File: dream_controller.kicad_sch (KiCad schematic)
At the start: 5 parts, among them J1 Conn_01x02_Male, J2 Conn_01x02_Male, U1 RP2040, U2 MCP2518FDT-H/SL, U3 MCP2561FD-E/SN

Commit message: added power
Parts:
- removed U2: MCP2518FDT-H/SL, SOIC14_150MIL_SL_MCH, symbol CAN IC:MCP2518FDT-H/SL
- removed U3: MCP2561FD-E/SN, SOIC8-N_MC_MCH, symbol TRANSCEIVER:MCP2561FD-E/SN
- added C1: 100u, symbol Device:C
- added C10, C?: 1u, symbol Device:C
- added C2, C3, C4, C5, C6, C7, C8, C9, C? (x2): 100n, symbol Device:C
- added R1: 1k, symbol Device:R_US
- added U2: W25Q32JVSS, Package_SO:SOIC-8_5.23x5.23mm_P1.27mm, symbol Memory_Flash:W25Q32JVSS
- added U3: MCP2518FDT-H/SL, SOIC14_150MIL_SL_MCH, symbol CAN IC:MCP2518FDT-H{brace}slash}SL
- added U4: MAX3051, symbol Interface_UART:MAX3051
- U1: footprint IC57_RP2040 -> RP2040_minimal:RP2040-QFN-56
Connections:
- net +3V3: now also U1.1 (IOVDD), U1.10 (IOVDD), U1.22 (IOVDD), U1.33 (IOVDD), U1.42 (IOVDD), U1.43 (ADC_AVDD), U1.44 (VREG_IN), U1.48 (USB_VDD), U1.49 (IOVDD), C1.1, C10.1, C2.1, C3.1, C4.1, C5.1, C6.1, C7.1, C8.1, C9.1, R1.1, U2.8 (VCC), U3.14 (VDD), U4.3 (VDD)
- net GND: now also U1.19 (TESTEN), U1.57 (GND), C1.2, C10.2, C2.2, C3.2, C4.2, C5.2, C6.2, C7.2, C8.2, C9.2, C?.2, C?.2, C?.2, U2.4 (GND), U3.7 (VSS), U4.2 (GND)
- net H_CAN: now also U4.7 (CANH)
- net L_CAN: now also U4.6 (CANL)
- net RX_CAN: now also U3.2 (RXCAN), U4.4 (RXD)
- net STBY: now also U3.9 (*INT0/GPIO0/XSTBY)
- net TX_CAN: now also U3.1 (TXCAN), U4.1 (TXD)
- net +1V1: now reaches U1.23 (DVDD)
- net +1V1: now also U1.45 (VREG_VOUT), U1.50 (DVDD), C?.1, C?.1, C?.1
- net F_D3: now reaches U1.51 (QSPI_SD3)
- net F_D3: now also U2.7 (IO3)
- net F_CLK: now reaches U1.52 (QSPI_SCLK)
- net F_CLK: now also U2.6 (CLK)
- net F_D0: now reaches U1.53 (QSPI_SD0)
- net F_D0: now also U2.5 (DI(IO0))
- net F_D2: now reaches U1.54 (QSPI_SD2)
- net F_D2: now also U2.3 (IO2)
- net F_D1: now reaches U1.55 (QSPI_SD1)
- net F_D1: now also U2.2 (DO(IO1))
- net SS: now reaches U1.56 (QSPI_SS)
- net SS: now also R1.2, U2.1 (~{CS})
- new net SHUTDOWN: U4.5 (SHDN)
- new net STANDBY: U4.8 (RS)

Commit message: update
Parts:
- added C14, C15: 14p, symbol Device:C
- added R1, R2: 27, symbol Device:R_US
- added Y1: Crystal, symbol Device:Crystal
- gave numbers to parts that had none: 3
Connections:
- net GND: now also C14.1, C15.1
- net at U1.20 (XIN): now also C14.2, Y1.1
- net at U1.21 (XOUT): now also C15.2, Y1.2
- net at U1.46 (USB_DM): now also R2.2
- net at U1.47 (USB_DP): now also R1.1
- new net D_N: R2.1
- new net D_P: R1.2

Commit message: added power for RP2040
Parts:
- added C? (x3): 10u, symbol Device:C
- added J1: USB_B_Micro, symbol Connector:USB_B_Micro
- added U5: LM1117-3.3, symbol Regulator_Linear:LM1117-3.3
- added U6: MAX40200AUK, Package_TO_SOT_SMD:SOT-23-5, symbol Analog_Switch:MAX40200AUK
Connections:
- net +3V3: now also C?.1, U5.2 (VO)
- net GND: now also C?.2, C?.2, C?.2, J1.5 (GND), J1.6 (Shield), U5.1 (GND), U6.2 (GND)
- net INHA: now reaches U1.2 (GPIO0)
- net INHB: now reaches U1.3 (GPIO1)
- net INLA: now reaches U1.4 (GPIO2)
- net INLB: now reaches U1.5 (GPIO3)
- net D_N renamed USB_D-
- net USB_D-: now also J1.2 (D-)
- net D_P renamed USB_D+
- net USB_D+: now also J1.3 (D+)
- new net: C?.1, J1.1 (VBUS), U6.1 (VDD), U6.3 (EN)
- new net VCC: C?.1, U5.3 (VI), U6.5 (OUT)
- no-connect marks 0 -> 1
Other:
- added sheet Driver (driver.kicad_sch)
- moved on the sheet: C1, R1, U2

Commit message: finished schematic design
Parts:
- removed C2, C3: 100n, symbol Device:C
- removed J1, J2: Conn_01x02_Male, symbol Connector:Conn_01x02_Male
- removed U3: MCP2518FDT-H/SL, SOIC14_150MIL_SL_MCH, symbol CAN IC:MCP2518FDT-H{brace}slash}SL
- removed U4: MAX3051, symbol Interface_UART:MAX3051
- added J2: Conn_01x04_Male, symbol Connector:Conn_01x04_Male
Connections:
- net INHA: now also U1.34 (GPIO22); no longer U1.2 (GPIO0)
- net INHB: now also U1.35 (GPIO23); no longer U1.3 (GPIO1)
- net INLA: now also U1.36 (GPIO24); no longer U1.4 (GPIO2)
- net INLB: now also U1.37 (GPIO25); no longer U1.5 (GPIO3)
- net CURRENT: now reaches U1.38 (GPIO26_ADC0)
- new net SPI_CLK: J2.2 (Pin_2), U1.4 (GPIO2)
- new net SPI_CS: J2.1 (Pin_1), U1.3 (GPIO1)
- new net SPI_MISO: J2.4 (Pin_4), U1.5 (GPIO3)
- new net SPI_MOSI: J2.3 (Pin_3), U1.2 (GPIO0)

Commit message: assigned footprints and started PCB
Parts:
- C1, C10, C11, C12, C13, C14, C15, C4, C5, C6, C7, C8, C9, R1, R2: footprint (none) -> Capacitor_SMD:C_0603_1608Metric
- C17, C2, C3: renamed from C?; footprint (none) -> Capacitor_SMD:C_0603_1608Metric
- J1: footprint (none) -> Connector_USB:USB_Micro-B_Amphenol_10118194_Horizontal
- J2: footprint (none) -> Connector_JST:JST_XH_B4B-XH-A_1x04_P2.50mm_Vertical
- R3: renamed from R1; footprint (none) -> Capacitor_SMD:C_0603_1608Metric
- U1: footprint RP2040_minimal:RP2040-QFN-56 -> RP2040:RP2040-QFN-56
- U5: footprint (none) -> Package_TO_SOT_SMD:SOT-223
- Y1: footprint (none) -> Crystal:Crystal_SMD_3225-4Pin_3.2x2.5mm
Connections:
- net XIN: now reaches C14.2, U1.20 (XIN), Y1.1
- net XOUT: now reaches C15.2, U1.21 (XOUT), Y1.2
- net VBUS: now reaches C2.1, J1.1 (VBUS), U6.1 (VDD), U6.3 (EN)
- net VCC renamed +15V

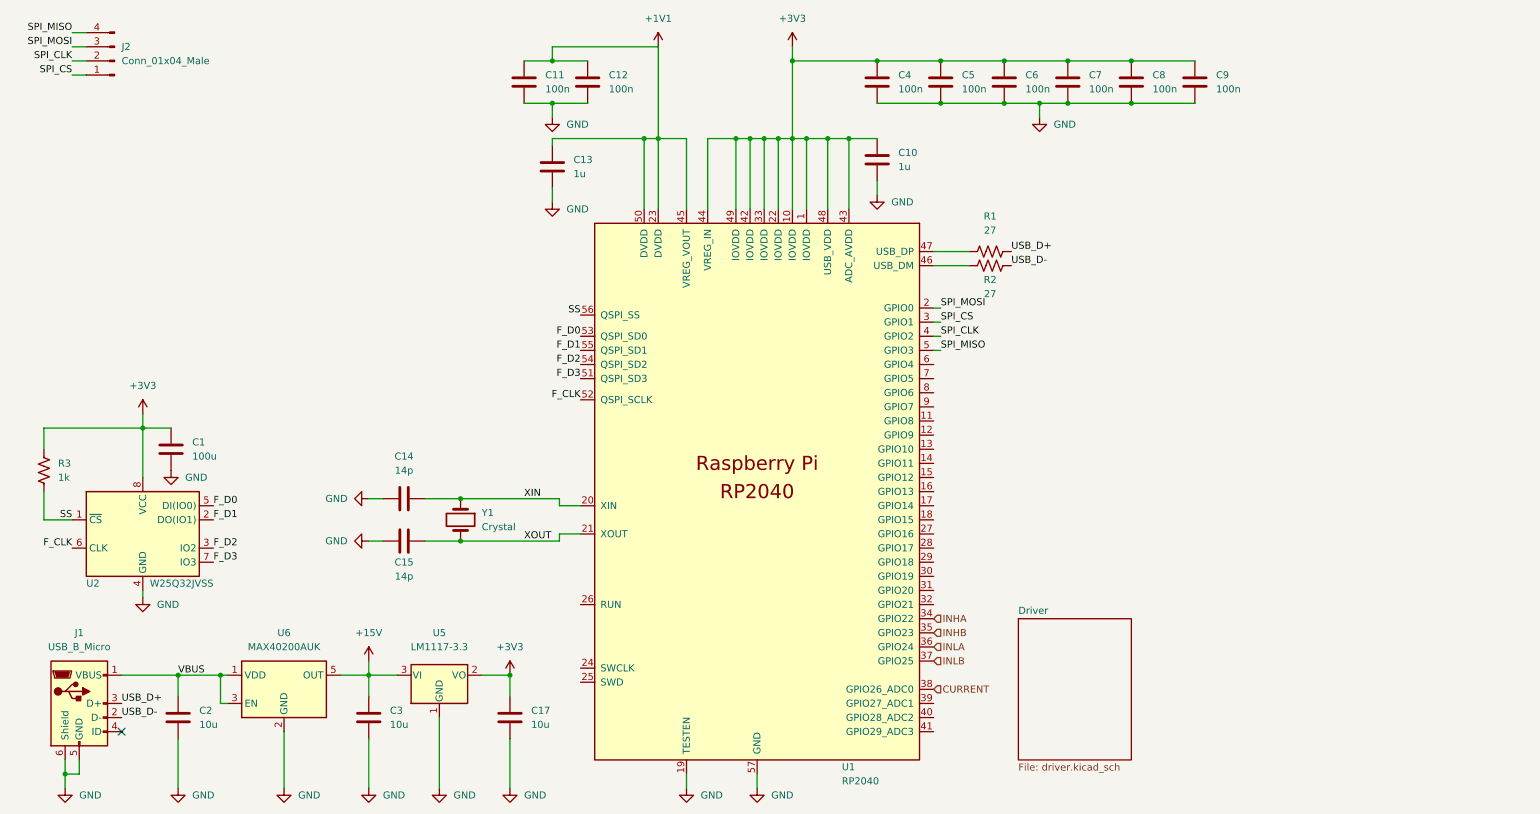
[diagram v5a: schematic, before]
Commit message: updating to CAN
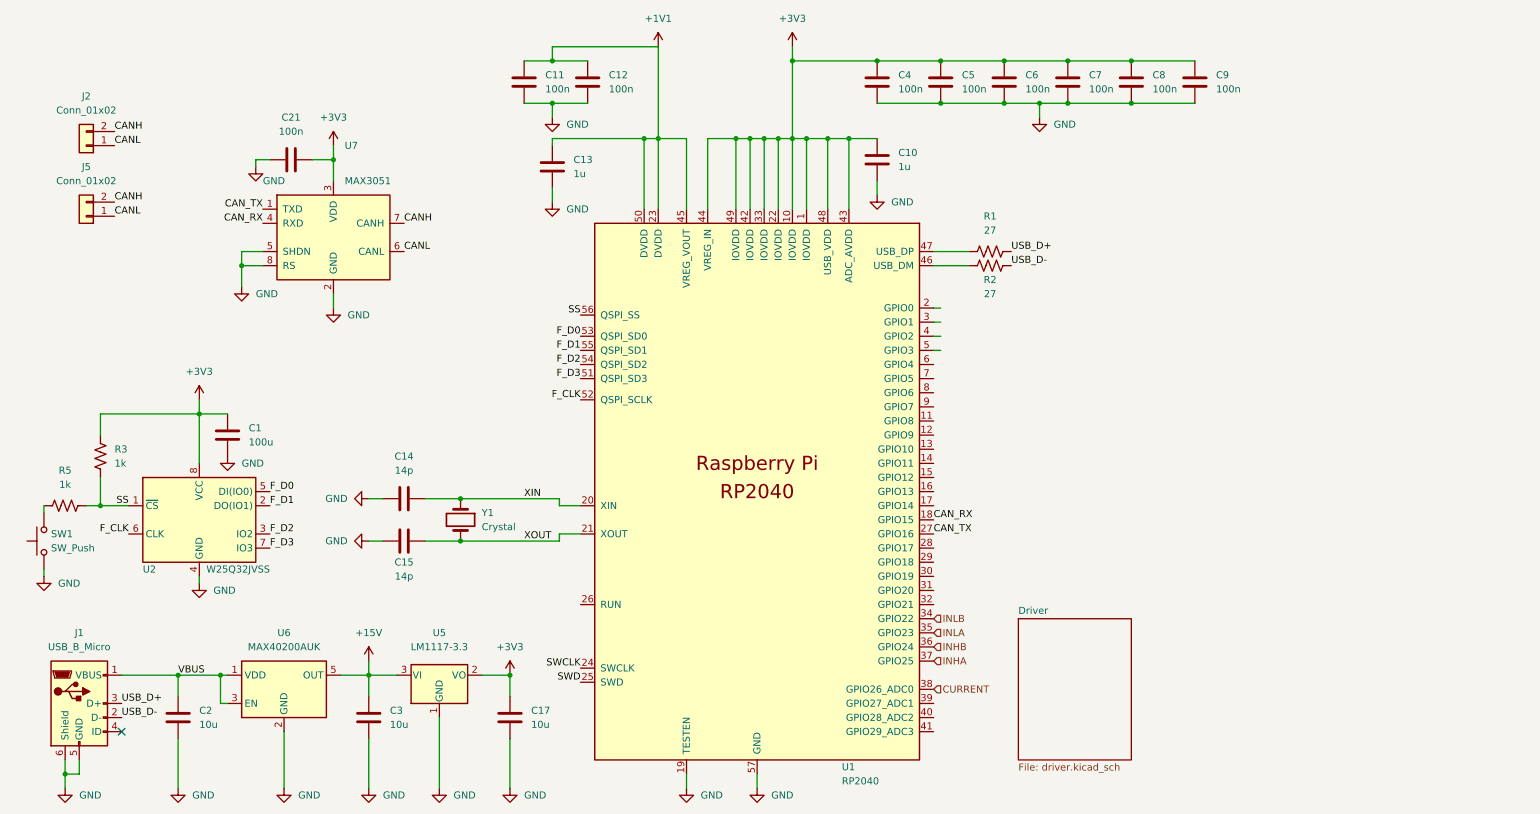
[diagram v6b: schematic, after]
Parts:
- removed J2: Conn_01x04_Male, Connector_JST:JST_XH_B4B-XH-A_1x04_P2.50mm_Vertical, symbol Connector:Conn_01x04_Male
- added C21: 100n, Capacitor_SMD:C_0402_1005Metric, symbol Device:C
- added J2, J5: Conn_01x02, symbol Connector_Generic:Conn_01x02
- added R5: 1k, Resistor_SMD:R_0603_1608Metric, symbol Device:R_US
- added SW1: SW_Push, RP2040:PTS636, symbol Switch:SW_Push
- added U7: MAX3051, Package_SO:SOIC-8_3.9x4.9mm_P1.27mm, symbol Interface_UART:MAX3051
- C10, C11, C12, C13, C14, C15, C4, C5, C6, C7, C8, C9, R1, R2, R3: footprint Capacitor_SMD:C_0603_1608Metric -> Capacitor_SMD:C_0402_1005Metric
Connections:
- net +3V3: now also C21.2, U7.3 (VDD)
- net GND: now also C21.1, SW1.1, U7.2 (GND), U7.5 (SHDN), U7.8 (RS)
- net INHA: now also U1.37 (GPIO25); no longer U1.34 (GPIO22)
- net INHB: now also U1.36 (GPIO24); no longer U1.35 (GPIO23)
- net INLA: now also U1.35 (GPIO23); no longer U1.36 (GPIO24)
- net INLB: now also U1.34 (GPIO22); no longer U1.37 (GPIO25)
- net SS: now also R5.2
- net CAN_RX: now reaches U1.18 (GPIO15)
- net CAN_RX: now also U7.4 (RXD)
- net SWCLK: now reaches U1.24 (SWCLK)
- net SWD: now reaches U1.25 (SWD)
- net CAN_TX: now reaches U1.27 (GPIO16)
- net CAN_TX: now also U7.1 (TXD)
- net SPI_CLK: no longer names the net of U1.4 (GPIO2)
- net SPI_CS: no longer names the net of U1.3 (GPIO1)
- net SPI_MISO: no longer names the net of U1.5 (GPIO3)
- net SPI_MOSI: no longer names the net of U1.2 (GPIO0)
- new net: R5.1, SW1.2
- new net CANH: J2.2 (Pin_2), J5.2 (Pin_2), U7.7 (CANH)
- new net CANL: J2.1 (Pin_1), J5.1 (Pin_1), U7.6 (CANL)
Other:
- moved on the sheet: C1, R3, U2

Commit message: continued CANification
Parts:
- removed U6: MAX40200AUK, Package_TO_SOT_SMD:SOT-23-5, symbol Analog_Switch:MAX40200AUK
- added D1: D, Diode_SMD:D_0603_1608Metric, symbol Device:D
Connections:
- net +15V: now also D1.1 (K)
- net VBUS: now also D1.2 (A)
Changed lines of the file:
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@@
   (junction (at 162.56 35.56) (diameter 0) (color 0 0 0 0)
-  )
-  (junction (at 49.53 132.08) (diameter 0) (color 0 0 0 0)
   )
   (junction (at 190.5 21.59) (diameter 0) (color 0 0 0 0)
@@
     (stroke (width 0) (type default) (color 0 0 0 0))
   )
-  (wire (pts (xy 60.96 142.24) (xy 60.96 152.4))
-    (stroke (width 0) (type default) (color 0 0 0 0))
-  )
-  (wire (pts (xy 49.53 132.08) (xy 50.8 132.08))
+  (wire (pts (xy 41.91 132.08) (xy 57.15 132.08))
     (stroke (width 0) (type default) (color 0 0 0 0))
   )
@@
     (stroke (width 0) (type default) (color 0 0 0 0))
   )
-  (wire (pts (xy 50.8 137.16) (xy 49.53 137.16))
-    (stroke (width 0) (type default) (color 0 0 0 0))
-  )
-  (wire (pts (xy 71.12 132.08) (xy 76.2 132.08))
+  (wire (pts (xy 64.77 132.08) (xy 76.2 132.08))
     (stroke (width 0) (type default) (color 0 0 0 0))
   )
@@
     (stroke (width 0) (type default) (color 0 0 0 0))
   )
-  (wire (pts (xy 49.53 132.08) (xy 49.53 137.16))
-    (stroke (width 0) (type default) (color 0 0 0 0))
-  )
   (wire (pts (xy 76.2 129.54) (xy 76.2 132.08))
     (stroke (width 0) (type default) (color 0 0 0 0))
   )
   (wire (pts (xy 109.22 19.05) (xy 128.27 19.05))
-    (stroke (width 0) (type default) (color 0 0 0 0))
-  )
-  (wire (pts (xy 41.91 132.08) (xy 49.53 132.08))
     (stroke (width 0) (type default) (color 0 0 0 0))
   )
@@
     (pin "2")
   )
+  (symbol (lib_id "Device:D") (at 60.96 132.08 180) (unit 1)
+    (in_bom yes) (on_board yes) (fields_autoplaced)
+    (property "Reference" "D1" (id 0) (at 60.96 125.73 0))
+    (property "Value" "D" (id 1) (at 60.96 128.27 0))
+    (property "Footprint" "Diode_SMD:D_0603_1608Metric" (id 2) (at 60.96 132.08 0)
+      (effects (font (size 1.27 1.27)) hide)
+    )
+    (property "Datasheet" "~" (id 3) (at 60.96 132.08 0)
+      (effects (font (size 1.27 1.27)) hide)
+    )
+    (pin "1")
+    (pin "2")
+  )
   (symbol (lib_id "Device:C") (at 224.79 25.4 0) (unit 1)
     (in_bom yes) (on_board yes) (fields_autoplaced)
@@
     (pin "2")
   )
-  (symbol (lib_id "Analog_Switch:MAX40200AUK") (at 60.96 134.62 0) (unit 1)
-    (in_bom yes) (on_board yes) (fields_autoplaced)
-    (property "Reference" "U6" (id 0) (at 60.96 124.46 0))
-    (property "Value" "MAX40200AUK" (id 1) (at 60.96 127 0))
-    (property "Footprint" "Package_TO_SOT_SMD:SOT-23-5" (id 2) (at 60.96 121.92 0)
-      (effects (font (size 1.27 1.27)) hide)
-    )
-    (property "Datasheet" "https://datasheets.maximintegrated.com/en/ds/MAX40200.pdf" (id 3) (at 60.96 121.92 0)
-      (effects (font (size 1.27 1.27)) hide)
-    )
-    (pin "1")
-    (pin "2")
-    (pin "3")
-    (pin "4")
-    (pin "5")
-  )
   (symbol (lib_id "power:+3V3") (at 69.85 36.83 0) (unit 1)
     (in_bom yes) (on_board yes) (fields_autoplaced)
@@
     (pin "5")
     (pin "6")
-  )
-  (symbol (lib_id "power:GND") (at 60.96 152.4 0) (unit 1)
-    (in_bom yes) (on_board yes) (fields_autoplaced)
-    (property "Reference" "#PWR0109" (id 0) (at 60.96 158.75 0)
-      (effects (font (size 1.27 1.27)) hide)
-    )
-    (property "Value" "GND" (id 1) (at 63.5 153.6699 0)
-      (effects (font (size 1.27 1.27)) (justify left))
-    )
-    (property "Footprint" "" (id 2) (at 60.96 152.4 0)
-      (effects (font (size 1.27 1.27)) hide)
-    )
-    (property "Datasheet" "" (id 3) (at 60.96 152.4 0)
-      (effects (font (size 1.27 1.27)) hide)
-    )
-    (pin "1")
   )
   (symbol (lib_id "power:GND") (at 45.72 115.57 0) (unit 1)
@@
       (reference "#PWR0108") (unit 1) (value "+3V3") (footprint "")
     )
-    (path "/9e6a4a07-6dfb-4da1-a0e7-9495dae995b8"
-      (reference "#PWR0109") (unit 1) (value "GND") (footprint "")
-    )
     (path "/39c99db7-0f1f-414b-b1e8-9f0278f24f79"
       (reference "#PWR0110") (unit 1) (value "GND") (footprint "")
@@
       (reference "C21") (unit 1) (value "100n") (footprint "Capacitor_SMD:C_0402_1005Metric")
     )
+    (path "/5a6287cc-e2c6-4796-ac1a-100d7e922017"
+      (reference "D1") (unit 1) (value "D") (footprint "Diode_SMD:D_0603_1608Metric")
+    )
     (path "/9dd782f8-4e0a-4a92-8a8f-83c306aedc9f"
       (reference "J1") (unit 1) (value "USB_B_Micro") (footprint "Connector_USB:USB_Micro-B_Amphenol_10118194_Horizontal")
@@
       (reference "U5") (unit 1) (value "LM1117-3.3") (footprint "Package_TO_SOT_SMD:SOT-223")
     )
-    (path "/8c548cbd-08ae-4ab4-b4c0-22801cccd939"
-      (reference "U6") (unit 1) (value "MAX40200AUK") (footprint "Package_TO_SOT_SMD:SOT-23-5")
-    )
     (path "/6f3bdcf1-177f-488b-8896-43a58c46b687"
